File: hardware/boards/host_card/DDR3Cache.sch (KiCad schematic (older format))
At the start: 8 parts, among them U1 ECP5UM5G-381caBGA, U4 IS43TR16256B-125KBL, U8 IS43TR16256B-125KBL, X2 AX3

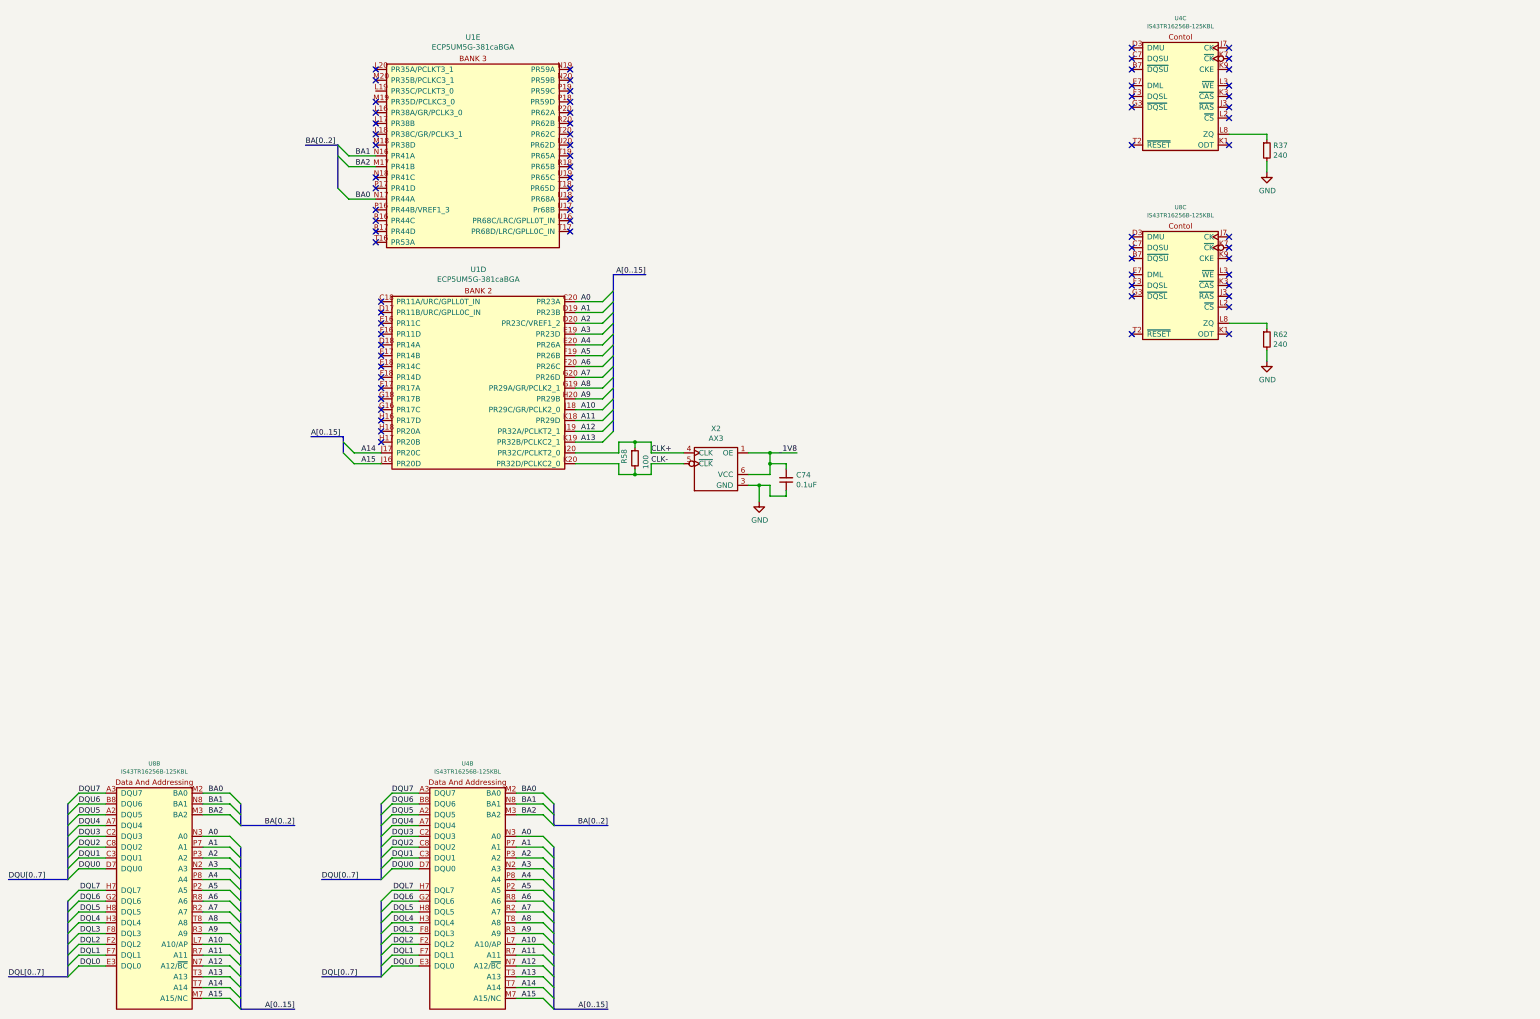
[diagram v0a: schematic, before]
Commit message: Moving some things around in  the DDR3 cache schematic
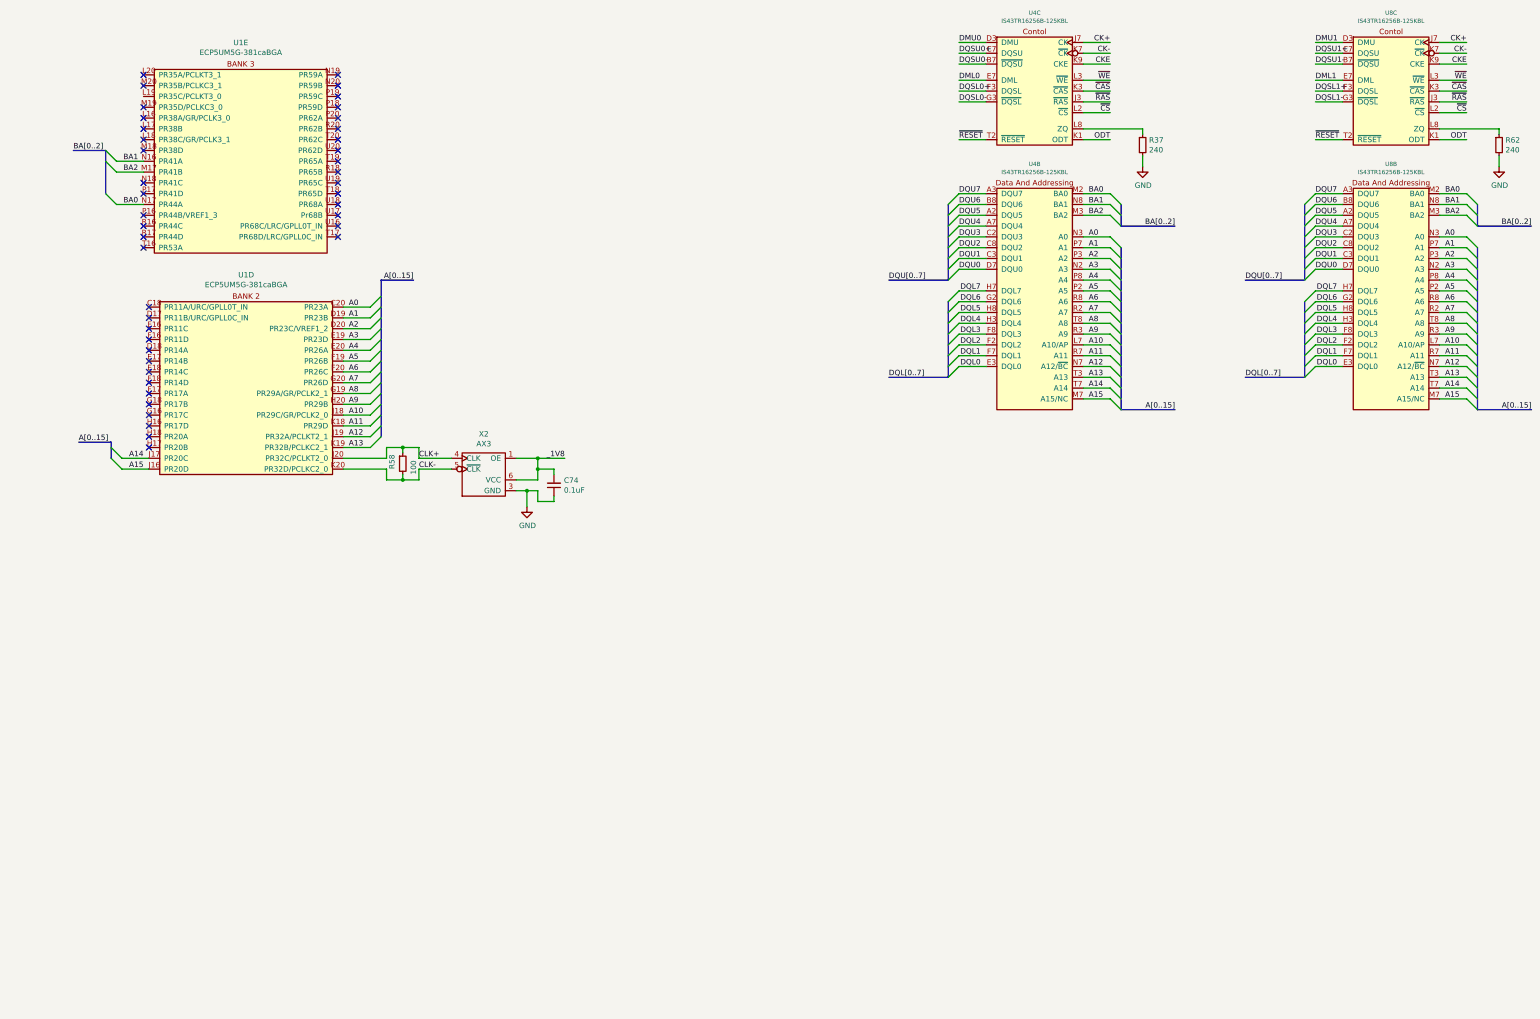
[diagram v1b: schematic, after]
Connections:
- net DQSU0-: now reaches U4.B7 (~DQSU)
- net DQSU0+: now reaches U4.C7 (DQSU)
- net DMU0: now reaches U4.D3 (DMU)
- net DML0: now reaches U4.E7 (DML)
- net DQSL0+: now reaches U4.F3 (DQSL)
- net DQSL0-: now reaches U4.G3 (~DQSL)
- net ~RAS: now reaches U4.J3 (~RAS)
- net ~RAS: now also U8.J3 (~RAS)
- net CK+: now reaches U4.J7 (CK)
- net CK+: now also U8.J7 (CK)
- net ODT: now reaches U4.K1 (ODT)
- net ODT: now also U8.K1 (ODT)
- net ~CAS: now reaches U4.K3 (~CAS)
- net ~CAS: now also U8.K3 (~CAS)
- net CK-: now reaches U4.K7 (~CK)
- net CK-: now also U8.K7 (~CK)
- net CKE: now reaches U4.K9 (CKE)
- net CKE: now also U8.K9 (CKE)
- net ~CS: now reaches U4.L2 (~CS)
- net ~CS: now also U8.L2 (~CS)
- net ~WE: now reaches U4.L3 (~WE)
- net ~WE: now also U8.L3 (~WE)
- net ~RESET: now reaches U4.T2 (~RESET)
- net ~RESET: now also U8.T2 (~RESET)
- net DQSU1-: now reaches U8.B7 (~DQSU)
- net DQSU1+: now reaches U8.C7 (DQSU)
- net DMU1: now reaches U8.D3 (DMU)
- net DML1: now reaches U8.E7 (DML)
- net DQSL1+: now reaches U8.F3 (DQSL)
- net DQSL1-: now reaches U8.G3 (~DQSL)
- no-connect marks 73 -> 43
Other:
- moved on the sheet: C74, R37, R58, R62, U1D, U1E, U4B, U4C, U8B, U8C, X2

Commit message: Some updates with the DDR3, gonna need to re-assign most of the pins to make routing it not a massive pain in the ass
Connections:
- net DML1 is gone; now on net DML0: U8.E7 (DML)
- net DMU1 is gone; now on net DMU0: U8.D3 (DMU)
- net DQSL1+ is gone; now on net DQSL0+: U8.F3 (DQSL)
- net DQSL1- is gone; now on net DQSL0-: U8.G3 (~DQSL)
- net DQSU1+ is gone; now on net DQSU0+: U8.C7 (DQSU)
- net DQSU1- is gone; now on net DQSU0-: U8.B7 (~DQSU)
- net A0: now also U1.K20 (PR32D/PCLKC2_0); no longer U1.C20 (PR23A)
- net A1: now also U1.J20 (PR32C/PCLKT2_0); no longer U1.D19 (PR23B)
- net A10: now also U1.H18 (PR20A); no longer U1.J18 (PR29C/GR/PCLK2_0)
- net A11: now also U1.H16 (PR17D); no longer U1.K18 (PR29D)
- net A12: now also U1.G16 (PR17C); no longer U1.J19 (PR32A/PCLKT2_1)
- net A13: now also U1.G18 (PR17B); no longer U1.K19 (PR32B/PCLKC2_1)
- net A14: now also U1.F17 (PR17A); no longer U1.J17 (PR20C)
- net A15: now also U1.F18 (PR14D); no longer U1.J16 (PR20D)
- net A2: now also U1.K19 (PR32B/PCLKC2_1); no longer U1.D20 (PR23C/VREF1_2)
- net A3: now also U1.J19 (PR32A/PCLKT2_1); no longer U1.E19 (PR23D)
- net A4: now also U1.K18 (PR29D); no longer U1.E20 (PR26A)
- net A5: now also U1.F20 (PR26C); no longer U1.F19 (PR26B)
- net A6: no longer U1.F20 (PR26C)
- net A7: now also U1.J16 (PR20D); no longer U1.G20 (PR26D)
- net A8: now also U1.J17 (PR20C); no longer U1.G19 (PR29A/GR/PCLK2_1)
- net A9: now also U1.H17 (PR20B); no longer U1.H20 (PR29B)
- net BA0: no longer U1.N17 (PR44A)
- net BA1: now also U1.C20 (PR23A); no longer U1.N16 (PR41A)
- net BA2: now also U1.D19 (PR23B); no longer U1.M17 (PR41B)
- net CLK+: now also U1.L20 (PR35A/PCLKT3_1); no longer U1.J20 (PR32C/PCLKT2_0)
- net CLK-: now also U1.M20 (PR35B/PCLKC3_1); no longer U1.K20 (PR32D/PCLKC2_0)
- net DQL0: now also U1.M19 (PR35D/PCLKC3_0)
- net DQL1: now also U1.L16 (PR38A/GR/PCLK3_0)
- net DQL2: now also U1.L18 (PR38C/GR/PCLK3_1)
- net DQL3: now also U1.M18 (PR38D)
- net DQL4: now also U1.N18 (PR41C)
- net DQL5: now also U1.N17 (PR44A)
- net DQL6: now also U1.R17 (PR44D)
- net DQL7: now also U1.R16 (PR44C)
- net DQSL0+: now also U1.N16 (PR41A)
- net DQSL0-: now also U1.M17 (PR41B)
- net DQSU0+: now also U1.T19 (PR65A)
- net DQSU0-: now also U1.R18 (PR65B)
- net DQU0: now also U1.P19 (PR59C)
- net DQU1: now also U1.P18 (PR59D)
- net DQU2: now also U1.P20 (PR62A)
- net DQU3: now also U1.R20 (PR62B)
- net DQU4: now also U1.U20 (PR62D)
- net DQU5: now also U1.U19 (PR65C)
- net DQU6: now also U1.U18 (PR68A)
- net DQU7: now also U1.U17 (Pr68B)
- net ~CAS: now also U1.E19 (PR23D)
- net ~RAS: now also U1.D20 (PR23C/VREF1_2)
- net ~WE: now also U1.E20 (PR26A)
- net ~CS0: now reaches U1.N19 (PR59A)
- net ~CS0: now also U4.L2 (~CS)
- net ~CS1: now reaches U1.N20 (PR59B)
- net ~CS1: now also U8.L2 (~CS)
- net ODT1: now reaches U1.T16 (PR53A)
- net ODT1: now also U8.K1 (ODT)
- net CKE renamed CKE0
- net CKE0: now also U1.F19 (PR26B); no longer U8.K9 (CKE)
- net ODT renamed ODT0
- net ODT0: now also U1.J18 (PR29C/GR/PCLK2_0); no longer U8.K1 (ODT)
- removed net ~CS: U4.L2 (~CS), U8.L2 (~CS)
- new net CKE1: U1.G20 (PR26D), U8.K9 (CKE)
- no-connect marks 43 -> 0
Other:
- note added: "As Divined By Lattice Diamond\n"
- note added: "FIX SYMBOL, ADD K16"
- note added: "FIX SYMBOL, ADD K17"
- note added: "Wat do with these?\n"
- note added: "~WE~ -> E20\n~RAS ~ -> D20\nODT1 -> T16\nODT0 -> J18\nCKE1 -> G20\nCKE0 -> F19\n~CAS ~ -> E19\nBA2 -> D19\nBA1 -> C20\nBA0 -> K17\nADDR15 -> F18 \nADDR14 -> F17\nADDR13 -> G18\nADDR12 -> G16\nADDR11 -> H16\nADDR10 -> H18\nADDR9 -> H17\nADDR8 -> J17\nADDR7 -> J16\nADDR6 -> K16\nADDR5 -> F20\nADDR4 -> K18\nADDR3 -> J19\nADDR2 -> K19\nADDR1 -> J20\nADDR0 -> K20\n\n~DQS1 ~ -> R18\nDQS1 -> T19\n~DQS0~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"
- moved on the sheet: C74, R58, U1D, U1E, X2

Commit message: Fixed  / updated the ECP5 symbol for the ECP5UM5G-85K
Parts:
- U1: symbol lethalbit:ECP5UM5G-381caBGA -> lethalbit:LFE5UM5G-85F-8BG381I
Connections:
- net A6: now also U1.K16 (PR29A)
- net BA0: now also U1.K17 (PR29B)
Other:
- note removed: "FIX SYMBOL, ADD K16"
- note removed: "FIX SYMBOL, ADD K17"
- moved on the sheet: C74, R58, X2

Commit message: Broke out the DDR3 modules and added the 0.75V LDO for the VREFCA and VREFDQ lines for each of the DDR3 modules
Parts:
- added C83: 10nF, Capacitor_SMD:C_0402_1005Metric, symbol Device:C_Small
- added R36, R8: 50, Resistor_SMD:R_0402_1005Metric, symbol Device:R_Small
- X2: value AX3 -> 100MHz
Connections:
- net CK+: now also U1.G19 (PR41A), R8.1
- net CK-: now also U1.H20 (PR41B), R36.1
- net DML0: now also U1.D17 (PR11B)
- net DMU0: now also U1.C18 (PR11A)
- net GND: now also C83.2
- net ~RESET renamed ~DDR_RESET
- new net: C83.1, R36.2, R8.2
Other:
- note added: "TODO: DDR3 Termination\n\n"
- note removed: "Wat do with these?\n"
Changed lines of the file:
@@
 AR Path="/5EDF3898/5FE30290" Ref="X2"  Part="1"
 F 0 "X2" H 3600 5375 50  0000 C CNN
-F 1 "AX3" H 3600 5284 50  0000 C CNN
+F 1 "100MHz" H 3600 5284 50  0000 C CNN
 F 2 "lethalbit:AX3" H 3250 5300 50  0001 C CNN
 F 3 "https://abracon.com/datasheets/AX3.pdf" H 3250 5300 50  0001 C CNN
@@
 A[0..15]
 Wire Wire Line
-	8200 4950 8450 4950
+	5050 3000 5300 3000
 Wire Wire Line
 	6650 5850 6250 5850
 Wire Wire Line
-	8200 5050 8450 5050
+	5050 3100 5300 3100
 Wire Wire Line
 	5000 5850 5350 5850
@@
 Wire Wire Line
 	5000 5950 5350 5950
-Text Label 8200 4950 0    50   ~ 0
+Text Label 5050 3000 0    50   ~ 0
 DMU0
 Text Label 6650 5850 2    50   ~ 0
@@
 Text Label 6650 5950 2    50   ~ 0
 DQSU0-
-Text Label 8200 5050 0    50   ~ 0
+Text Label 5050 3100 0    50   ~ 0
 DML0
 Text Label 5000 5850 0    50   ~ 0
@@
 ~CS0
 Wire Wire Line
-	8450 5200 8200 5200
-Wire Wire Line
-	8450 5300 8200 5300
-Text Label 8200 5200 0    50   ~ 0
+	6200 3900 6450 3900
+Wire Wire Line
+	6200 4000 6450 4000
+Text Label 6450 3900 2    50   ~ 0
 CK+
-Text Label 8200 5300 0    50   ~ 0
+Text Label 6450 4000 2    50   ~ 0
 CK-
-Text Notes 8050 4800 0    50   ~ 0
-Wat do with these?\n
 Wire Wire Line
 	5150 4950 5150 5150
@@
 Wire Wire Line
 	4500 4850 5250 4850
+Text Notes 5250 2550 0    50   ~ 0
+TODO: DDR3 Termination\n\n
+Wire Wire Line
+	9750 6150 9750 5750
+Text Label 9750 5750 3    50   ~ 0
+CK+
+Text Label 10050 5750 3    50   ~ 0
+CK-
+$Comp
+L Device:C_Small C?
+U 1 1 5F4CA25E
+P 9900 6700
+AR Path="/5EF66188/5F4CA25E" Ref="C?"  Part="1"
+AR Path="/5EDF3898/5F4CA25E" Ref="C83"  Part="1"
+F 0 "C83" H 9992 6746 50  0000 L CNN
+F 1 "10nF" H 9992 6655 50  0000 L CNN
+F 2 "Capacitor_SMD:C_0402_1005Metric" H 9900 6700 50  0001 C CNN
+F 3 "~" H 9900 6700 50  0001 C CNN
+F 4 "KEMET" H 9900 6700 50  0001 C CNN "MFR"
+F 5 "C0402C103M5RACTU" H 9900 6700 50  0001 C CNN "MPN"
+	1    9900 6700
+	1    0    0    -1
+$EndComp
+$Comp
+L power:GND #PWR0148
+U 1 1 5F4DD7B5
+P 9900 6950
+F 0 "#PWR0148" H 9900 6700 50  0001 C CNN
+F 1 "GND" H 9905 6777 50  0000 C CNN
+F 2 "" H 9900 6950 50  0001 C CNN
+F 3 "" H 9900 6950 50  0001 C CNN
+	1    9900 6950
+	1    0    0    -1
+$EndComp
+Wire Wire Line
+	9900 6800 9900 6950
+Wire Wire Line
+	9900 6600 9750 6600
+Wire Wire Line
+	9750 6600 9750 6350
+$Comp
+L Device:R_Small R?
+U 1 1 5F57684A
+P 9750 6250
+AR Path="/5EF66251/5F57684A" Ref="R?"  Part="1"
+AR Path="/5EDF3898/5F57684A" Ref="R8"  Part="1"
+F 0 "R8" H 9809 6296 50  0000 L CNN
+F 1 "50" H 9809 6205 50  0000 L CNN
+F 2 "Resistor_SMD:R_0402_1005Metric" H 9750 6250 50  0001 C CNN
+F 3 "~" H 9750 6250 50  0001 C CNN
+F 4 "Vishay Thin Film" H 9750 6250 50  0001 C CNN "MFR"
+F 5 "FC0402E50R0BST1" H 9750 6250 50  0001 C CNN "MPN"
+	1    9750 6250
+	1    0    0    -1
+$EndComp
+Wire Wire Line
+	10050 5750 10050 6150
+Wire Wire Line
+	10050 6350 10050 6600
+Wire Wire Line
+	10050 6600 9900 6600
+Connection ~ 9900 6600
+$Comp
+L Device:R_Small R?
+U 1 1 5F5BAC4B
+P 10050 6250
+AR Path="/5EF66251/5F5BAC4B" Ref="R?"  Part="1"
+AR Path="/5EDF3898/5F5BAC4B" Ref="R36"  Part="1"
+F 0 "R36" H 10109 6296 50  0000 L CNN
+F 1 "50" H 10109 6205 50  0000 L CNN
+F 2 "Resistor_SMD:R_0402_1005Metric" H 10050 6250 50  0001 C CNN
+F 3 "~" H 10050 6250 50  0001 C CNN
+F 4 "Vishay Thin Film" H 10050 6250 50  0001 C CNN "MFR"
+F 5 "FC0402E50R0BST1" H 10050 6250 50  0001 C CNN "MPN"
+	1    10050 6250
+	1    0    0    -1
+$EndComp
+Text HLabel 5900 2250 0    50   Input ~ 0
+~DDR_RESET
+Wire Wire Line
+	6150 2250 5900 2250
+Text Label 6150 2250 2    50   ~ 0
+~RESET
 Wire Bus Line
 	6550 2900 6550 3100
